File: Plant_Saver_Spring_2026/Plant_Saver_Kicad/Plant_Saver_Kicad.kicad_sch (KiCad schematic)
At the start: 23 parts, among them J2 StripboardConn, Q9 G09P02L, SW1 Select, SW2 Select, SW8 NK236WH, U1 CDBA140SL-HF, U2 CDBA140SL-HF, U3 CDBA140SL-HF, U4 CDBA140SL-HF, U5 ESP32-WROOM-32E-N16, U8 ESP32-WROOM-32D

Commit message: Misc. changes
Updated peripheral power switch, UI board connections
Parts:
- removed J2: StripboardConn, symbol Connector:Conn_01x08_Socket
- added J4, J6: B8B-PH-K-SLFSN, CONN_B8B-PH-K-S_JST, symbol B8B_PH_K_S_LF__SN_:B8B-PH-K-SLFSN
- added Q13: G09P02L, G09P02L:TSOT-23, symbol Simulation_SPICE:PMOS
- added R14: 150K, Resistor_THT:R_Axial_DIN0207_L6.3mm_D2.5mm_P10.16mm_Horizontal, symbol Device:R_US
- R10: value 150K -> 100K
- SW8: value NK236WH -> 25336NA; footprint NK236WH:SW_Slide-03_APEM-NK23GWH_10x9.2x2.6_P2.54mm -> 25336NA:SWITCH_25336NA_APM
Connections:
- net Error: now also J6.3
- net GND: now also J6.8, R14.2
- net Periph_EN: now also Q13.2 (G); no longer Q9.2 (G)
- net Vbus: now also Q13.3 (S)
- net at U5.11 (IO26): now also J6.4
- net at U5.12 (IO27): now also J6.5
- net at U5.13 (IO14): now also J6.6
- net at U5.14 (IO12): now also J6.7
- new net: Q13.1 (D), Q9.2 (G), R14.1
- new net Interface Stripboard/Chg_Cpt_Lt: J4.2
- new net Interface Stripboard/Chg_Lt: J4.1
- new net Interface Stripboard/Chg_Scr_Btn: J4.6
- new net Interface Stripboard/Down_Btn: J4.5
- new net Interface Stripboard/Error_Lt: J4.3
- new net Interface Stripboard/GND: J4.8
- new net Interface Stripboard/Sel_Btn: J4.7
- new net Interface Stripboard/Up_Btn: J4.4
- new net STAT1: J6.1
- new net STAT2: J6.2
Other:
- sheet Interface Stripboard ports: added Chg_Cpt_Lt, Chg_Lt, Chg_Scr_Btn, Down_Btn, Error_Lt, GND, Sel_Btn, Up_Btn; removed none
- note removed: "This is Dumb, Replace w/ NMOS on negative side"
- moved on the sheet: U8

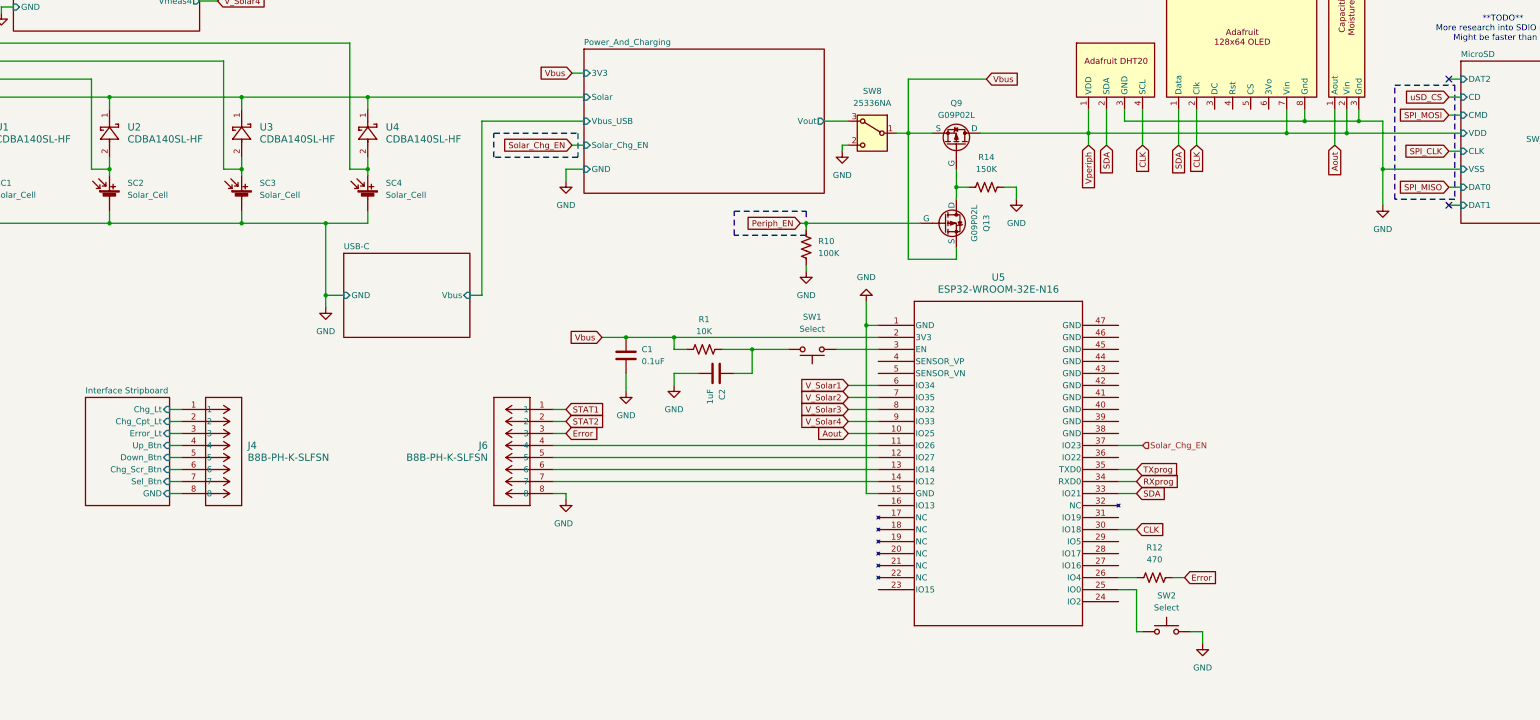
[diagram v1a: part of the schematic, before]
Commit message: Misc. fixes to schematic
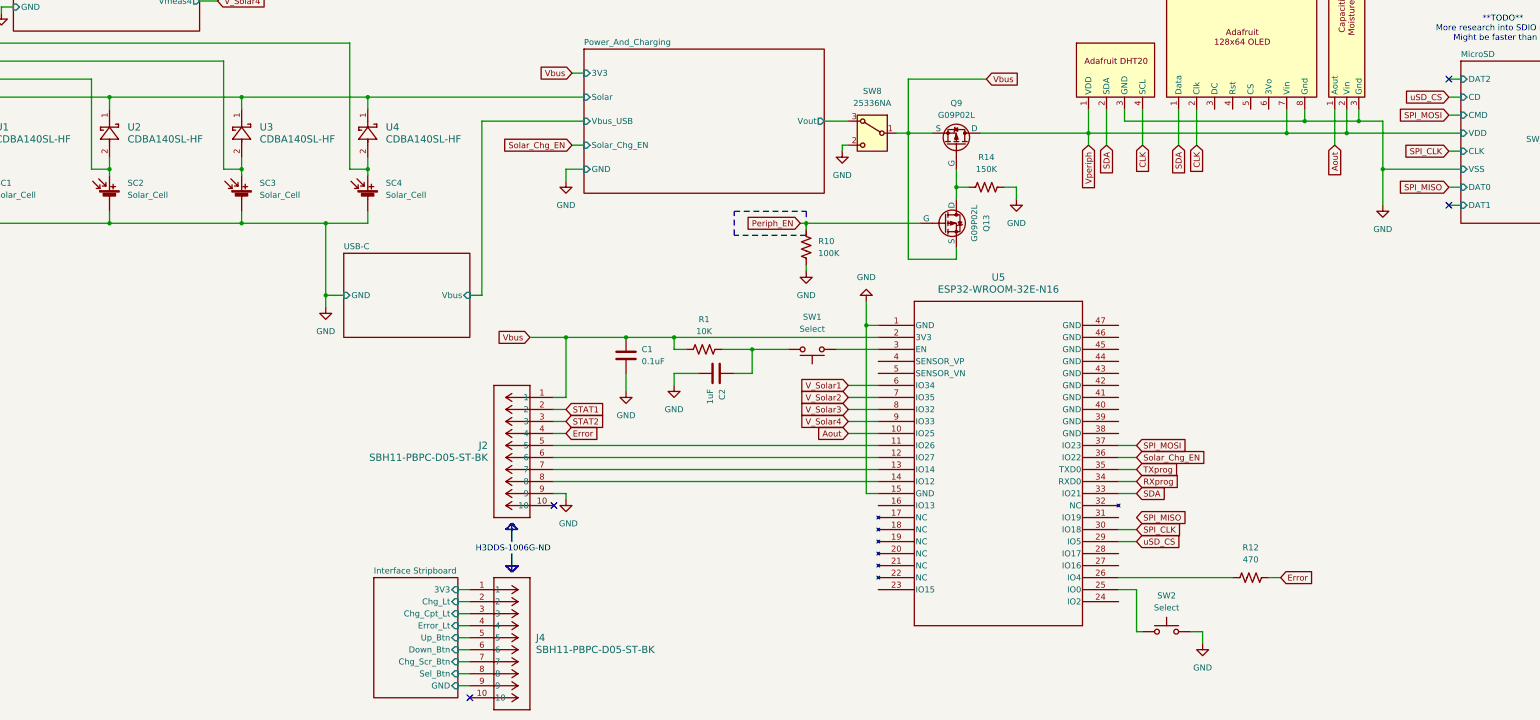
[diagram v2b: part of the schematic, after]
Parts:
- removed J4, J6: B8B-PH-K-SLFSN, CONN_B8B-PH-K-S_JST, symbol B8B_PH_K_S_LF__SN_:B8B-PH-K-SLFSN
- added J2, J4: SBH11-PBPC-D05-ST-BK, CONN_SBH11-PBPC-D05-ST-BK_SUL, symbol SBH11_PBPC_D05_ST_BK:SBH11-PBPC-D05-ST-BK
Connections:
- net CLK: no longer U5.30 (IO18)
- net Error: now also J2.4
- net GND: now also J2.9
- net Interface Stripboard/Chg_Cpt_Lt: now also J4.3
- net Interface Stripboard/Chg_Lt: now also J4.2
- net Interface Stripboard/Chg_Scr_Btn: now also J4.7
- net Interface Stripboard/Down_Btn: now also J4.6
- net Interface Stripboard/Error_Lt: now also J4.4
- net Interface Stripboard/GND: now also J4.9
- net Interface Stripboard/Sel_Btn: now also J4.8
- net Interface Stripboard/Up_Btn: now also J4.5
- net SPI_CLK: now also U5.30 (IO18)
- net SPI_MOSI: now also U5.37 (IO23)
- net STAT1: now also J2.2
- net STAT2: now also J2.3
- net Solar_Chg_EN: now also U5.36 (IO22); no longer U5.37 (IO23)
- net Vbus: now also J2.1
- net uSD_CS: now also U5.29 (IO5)
- net at U5.11 (IO26): now also J2.5
- net at U5.12 (IO27): now also J2.6
- net at U5.13 (IO14): now also J2.7
- net at U5.14 (IO12): now also J2.8
- new net Interface Stripboard/3V3: J4.1
- no-connect marks 2 -> 4
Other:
- sheet Interface Stripboard ports: added 3V3; removed none
- note added: "H3DDS-1006G-ND"
- moved on the sheet: R12

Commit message: Footprint updates
Misc. schematic fixes, mostly updated/added footprints where needed.
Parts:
- removed R12: 470, Resistor_THT:R_Axial_DIN0207_L6.3mm_D2.5mm_P10.16mm_Horizontal, symbol Device:R_US
- added C10: 0.1uF, Capacitor_THT:C_Disc_D4.7mm_W2.5mm_P5.00mm, symbol Device:C
- added C11: 10uF, Capacitor_THT:C_Disc_D4.7mm_W2.5mm_P5.00mm, symbol Device:C
- added J5: S3B-PH-K-S, Connector_JST:JST_PH_S3B-PH-K_1x03_P2.00mm_Horizontal, symbol Connector:Conn_01x03_Pin
- added J6, J7: SM04B-SRSS-TB, Connector_JST:JST_SH_SM04B-SRSS-TB_1x04-1MP_P1.00mm_Horizontal, symbol Connector:Conn_01x04_Pin
- SW1: value Select -> Reset; footprint (none) -> Button_Switch_THT:SW_PUSH_6mm
- SW2: value Select -> Boot; footprint (none) -> Button_Switch_THT:SW_PUSH_6mm
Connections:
- net Aout: now also J5.1 (Pin_1); no longer U9.1 (Aout)
- net CLK: now also J6.4 (Pin_4); no longer U7.2 (Clk)
- net Error: now also U5.26 (IO4)
- net GND: now also C2.1, SW1.1, C10.2, C11.2, J5.3 (Pin_3), J6.1 (Pin_1); no longer C2.2, U7.8 (Gnd), U9.3 (Gnd)
- net SDA: now also J6.3 (Pin_3); no longer U7.1 (Data)
- net Vbus: now also R1.2, C11.1; no longer R1.1
- net Vperiph: now also J5.2 (Pin_2), J6.2 (Pin_2); no longer U7.7 (Vin), U9.2 (Vin)
- net at U5.3 (EN): now also C2.2, R1.1, SW1.2, C10.1; no longer SW1.1
- new net: J7.1 (Pin_1), U7.8 (Gnd)
- new net: J7.2 (Pin_2), U7.7 (Vin)
- new net: J7.3 (Pin_3), U7.1 (Data)
- new net: J7.4 (Pin_4), U7.2 (Clk)
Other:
- sheet Power_And_Charging ports: added STAT1, STAT2; removed none
- note added: "1528-4210-ND"
- note added: "A03KR03KR26E152B"
- note added: "STEMMA QT Pinout: 1 [BLK] - GND 2 [RED] - Vcc 3 [BLU] - SDA 4 [YEL] - SCL"
- moved on the sheet: C1, C2, J2, J4, Q13, Q9, R1, R10, R14, SC1, SC2, SC3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

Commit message: Programming ports on schematic
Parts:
- removed U8: ESP32-WROOM-32D, RF_Module:ESP32-WROOM-32D, symbol RF_Module:ESP32-WROOM-32D
- added J8: Conn_01x06_Socket, Connector_PinSocket_2.54mm:PinSocket_1x06_P2.54mm_Vertical, symbol Connector:Conn_01x06_Socket
- added J9: Conn_01x02_Pin, Connector_PinHeader_2.54mm:PinHeader_1x02_P2.54mm_Vertical, symbol Connector:Conn_01x02_Pin
- added R19: 10K, Resistor_THT:R_Axial_DIN0207_L6.3mm_D2.5mm_P10.16mm_Horizontal, symbol Device:R_US
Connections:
- net GND: now also J8.1 (Pin_1), R19.1
- net Periph_EN: now also U5.28 (IO17)
- net SPI_MISO: now also U5.31 (IO19)
- net Solar_Chg_EN: now also U5.16 (IO13); no longer U5.36 (IO22)
- net Vbus: now also J9.1 (Pin_1)
- net uSD_DET: now also U5.27 (IO16)
- net at U5.24 (IO2): now also R19.2
- net CLK renamed SCL
- net SCL: now also U5.36 (IO22)
- net RXprog: no longer names the net of U5.34 (RXD0)
- net RXprog: now also J8.4 (Pin_4)
- net TXprog: no longer names the net of U5.35 (TXD0)
- net TXprog: now also J8.5 (Pin_5)
- new net: J8.3 (Pin_3), J9.2 (Pin_2)
- no-connect marks 4 -> 6
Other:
- note added: "FTDI Board Pinout: GND CTS Vcc Tx Rx DTR"
- note added: "Jumper for powering chip from FTDI"
- note removed: "**TODO** More research into SDIO needed Might be faster than SPI"
- note removed: "Most LIPO charging chips use current detection to end charging, since the battery will draw very little current when it's at full voltage. If the system load is also connected to that pin, it can throw that sensing out of wack since the current draw isn't only from the battery anymore."
- moved on the sheet: SW2

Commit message: Started PCB
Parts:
- added TP1, TP2, TP3, TP4, TP5, TP6: TestPoint, TestPoint:TestPoint_Pad_1.5x1.5mm, symbol Connector:TestPoint
- J2: footprint CONN_SBH11-PBPC-D05-ST-BK_SUL -> SBH11_PBPC_D05_ST_BK:CONN_SBH11-PBPC-D05-ST-BK_SUL
- U1, U2, U3, U4: footprint (none) -> CDBA140SL_HF:CDBA-HF
- renumbered C11 to C2, C2 to C3, C10 to C4, J4 to J1, J6 to J3, J7 to J4, J9 to J5, J8 to J6, J5 to J7, Q13 to Q1, Q9 to Q2, R10 to R2, R14 to R3, R19 to R4, SW8 to SW2, SW2 to SW3, U9 to U8
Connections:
- net GND: now also TP1.1
- net Power_And_Charging/Solar: now also TP2.1
- net SCL: now also TP4.1
- net SDA: now also TP3.1
- net at J6.4 (Pin_4), U5.34 (RXD0): now also TP6.1
- net at J6.5 (Pin_5), U5.35 (TXD0): now also TP5.1

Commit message: Refined PCB layout
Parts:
- added R44, R45: 10K, Resistor_SMD:R_1206_3216Metric_Pad1.30x1.75mm_HandSolder, symbol Device:R_US
- C1, C2, C3, C4: footprint Capacitor_THT:C_Disc_D4.7mm_W2.5mm_P5.00mm -> Capacitor_SMD:C_1206_3216Metric_Pad1.33x1.80mm_HandSolder
- R1, R2, R3, R4: footprint Resistor_THT:R_Axial_DIN0207_L6.3mm_D2.5mm_P10.16mm_Horizontal -> Resistor_SMD:R_1206_3216Metric_Pad1.30x1.75mm_HandSolder
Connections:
- net SCL: now also R44.2
- net SDA: now also R45.2
- net Vperiph: now also R44.1, R45.1
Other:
- moved on the sheet: J5, J6, TP3, TP4, TP5, TP6

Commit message: Began PCB routing
Routed solar input, measurement and protections
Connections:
- net GND: now also U5.38 (GND), U5.39 (GND), U5.40 (GND), U5.41 (GND), U5.42 (GND), U5.43 (GND), U5.44 (GND), U5.45 (GND), U5.46 (GND), U5.47 (GND)
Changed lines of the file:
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@@
 	)
 	(junction
+		(at 287.02 180.34)
+		(diameter 0)
+		(color 0 0 0 0)
+	)
+	(junction
 		(at 287.02 127)
 		(diameter 0)
@@
 	)
 	(junction
+		(at 287.02 162.56)
+		(diameter 0)
+		(color 0 0 0 0)
+	)
+	(junction
 		(at 302.26 124.46)
 		(diameter 0)
@@
 	)
 	(junction
+		(at 287.02 167.64)
+		(diameter 0)
+		(color 0 0 0 0)
+	)
+	(junction
 		(at 128.27 114.3)
 		(diameter 0)
@@
 	)
 	(junction
+		(at 287.02 177.8)
+		(diameter 0)
+		(color 0 0 0 0)
+	)
+	(junction
+		(at 287.02 165.1)
+		(diameter 0)
+		(color 0 0 0 0)
+	)
+	(junction
 		(at 193.04 167.64)
 		(diameter 0)
@@
 	)
 	(junction
+		(at 287.02 182.88)
+		(diameter 0)
+		(color 0 0 0 0)
+	)
+	(junction
+		(at 287.02 175.26)
+		(diameter 0)
+		(color 0 0 0 0)
+	)
+	(junction
 		(at 302.26 137.16)
 		(diameter 0)
@@
 	)
 	(junction
+		(at 287.02 172.72)
+		(diameter 0)
+		(color 0 0 0 0)
+	)
+	(junction
+		(at 287.02 170.18)
+		(diameter 0)
+		(color 0 0 0 0)
+	)
+	(junction
 		(at 73.66 114.3)
 		(diameter 0)
@@
 		)
 	)
+	(wire
+		(pts
+			(xy 287.02 180.34) (xy 287.02 177.8)
+		)
+		(stroke
+			(width 0)
+			(type default)
+		)
+	)
 	(polyline
 		(pts
@@
 	(wire
 		(pts
+			(xy 287.02 172.72) (xy 287.02 170.18)
+		)
+		(stroke
+			(width 0)
+			(type default)
+		)
+	)
+	(wire
+		(pts
 			(xy 134.62 238.76) (xy 137.16 238.76)
 		)
@@
 	(wire
 		(pts
+			(xy 287.02 160.02) (xy 292.1 160.02)
+		)
+		(stroke
+			(width 0)
+			(type default)
+		)
+	)
+	(wire
+		(pts
 			(xy 252.73 133.35) (xy 252.73 135.89)
 		)
@@
 		)
 	)
+	(wire
+		(pts
+			(xy 287.02 167.64) (xy 287.02 165.1)
+		)
+		(stroke
+			(width 0)
+			(type default)
+		)
+	)
 	(polyline
 		(pts
@@
 	(wire
 		(pts
+			(xy 287.02 165.1) (xy 287.02 162.56)
+		)
+		(stroke
+			(width 0)
+			(type default)
+		)
+	)
+	(wire
+		(pts
 			(xy 298.45 74.93) (xy 298.45 72.39)
 		)
@@
 	(wire
 		(pts
+			(xy 292.1 160.02) (xy 292.1 162.56)
+		)
+		(stroke
+			(width 0)
+			(type default)
+		)
+	)
+	(wire
+		(pts
 			(xy 303.53 74.93) (xy 298.45 74.93)
 		)
@@
 	(wire
 		(pts
+			(xy 287.02 177.8) (xy 287.02 175.26)
+		)
+		(stroke
+			(width 0)
+			(type default)
+		)
+	)
+	(wire
+		(pts
 			(xy 306.07 77.47) (xy 294.64 77.47)
 		)
@@
 	(wire
 		(pts
+			(xy 287.02 162.56) (xy 287.02 160.02)
+		)
+		(stroke
+			(width 0)
+			(type default)
+		)
+	)
+	(wire
+		(pts
 			(xy 134.62 223.52) (xy 137.16 223.52)
 		)
@@
 	(wire
 		(pts
+			(xy 287.02 170.18) (xy 287.02 167.64)
+		)
+		(stroke
+			(width 0)
+			(type default)
+		)
+	)
+	(wire
+		(pts
 			(xy 134.62 231.14) (xy 137.16 231.14)
 		)
@@
 	(wire
 		(pts
+			(xy 287.02 185.42) (xy 287.02 182.88)
+		)
+		(stroke
+			(width 0)
+			(type default)
+		)
+	)
+	(wire
+		(pts
 			(xy 154.94 190.5) (xy 236.22 190.5)
 		)
@@
 		)
 	)
+	(wire
+		(pts
+			(xy 287.02 175.26) (xy 287.02 172.72)
+		)
+		(stroke
+			(width 0)
+			(type default)
+		)
+	)
 	(polyline
 		(pts
@@
 		)
 	)
+	(wire
+		(pts
+			(xy 287.02 182.88) (xy 287.02 180.34)
+		)
+		(stroke
+			(width 0)
+			(type default)
+		)
+	)
 	(global_label "SCL"
 		(shape input)
@@
 					(unit 1)
 				)
+			)
+		)
+	)
+	(symbol
+		(lib_id "power:GND")
+		(at 292.1 162.56 0)
+		(unit 1)
+		(exclude_from_sim no)
+		(in_bom yes)
+		(on_board yes)
+		(dnp no)
+		(fields_autoplaced yes)
+		(property "Reference" "#PWR022"
+			(at 292.1 168.91 0)
+			(effects
+				(font
+					(size 1.27 1.27)
+				)
+				(hide yes)
+			)
+		)
+		(property "Value" "GND"
+			(at 292.1 167.64 0)
+			(effects
+				(font
+					(size 1.27 1.27)
+				)
+			)
+		)
+		(property "Footprint" ""
+			(at 292.1 162.56 0)
+			(effects
+				(font
+					(size 1.27 1.27)
+				)
+				(hide yes)
+			)
+		)
+		(property "Datasheet" ""
+			(at 292.1 162.56 0)
+			(effects
+				(font
+					(size 1.27 1.27)
+				)
+				(hide yes)
+			)
+		)
+		(property "Description" "Power symbol creates a global label with name \"GND\" , ground"
+			(at 292.1 162.56 0)
+			(effects
+				(font
+					(size 1.27 1.27)
+				)
+				(hide yes)
+			)
+		)
+		(pin "1"
+		)
+		(instances
+			(project "Plant_Saver_Kicad"
+				(path "/7f244634-d37a-4ff0-ba36-8027330ab1bd"
+					(reference "#PWR022")
+					(unit 1)
+				)

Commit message: Re-routed to fix issue on schematic
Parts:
- added J11: Test, Connector_PinHeader_2.54mm:PinHeader_1x02_P2.54mm_Vertical, symbol Connector:Conn_01x02_Socket
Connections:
- net Power_And_Charging/Vout: now also J11.2 (Pin_2)
- net Vbus: now also J11.1 (Pin_1)
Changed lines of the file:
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@@
 	)
 	(junction
+		(at 226.06 119.38)
+		(diameter 0)
+		(color 0 0 0 0)
+	)
+	(junction
 		(at 303.53 119.38)
 		(diameter 0)
@@
 	)
 	(junction
+		(at 240.03 121.92)
+		(diameter 0)
+		(color 0 0 0 0)
+	)
+	(junction
 		(at 101.6 114.3)
 		(diameter 0)
@@
 	(wire
 		(pts
+			(xy 226.06 119.38) (xy 229.87 119.38)
+		)
+		(stroke
+			(width 0)
+			(type default)
+		)
+	)
+	(wire
+		(pts
 			(xy 356.87 137.16) (xy 359.41 137.16)
 		)
@@
 	(wire
 		(pts
+			(xy 240.03 121.92) (xy 240.03 132.08)
+		)
+		(stroke
+			(width 0)
+			(type default)
+		)
+	)
+	(wire
+		(pts
 			(xy 289.56 229.87) (xy 313.69 229.87)
 		)
@@
 	(wire
 		(pts
-			(xy 224.79 119.38) (xy 229.87 119.38)
+			(xy 224.79 119.38) (xy 226.06 119.38)
 		)
 		(stroke
@@
 	(wire
 		(pts
+			(xy 240.03 132.08) (xy 236.22 132.08)
+		)
+		(stroke
+			(width 0)
+			(type default)
+		)
+	)
+	(wire
+		(pts
 			(xy 287.02 193.04) (xy 302.26 193.04)
 		)
@@
 	(wire
 		(pts
+			(xy 226.06 132.08) (xy 233.68 132.08)
+		)
+		(stroke
+			(width 0)
+			(type default)
+		)
+	)
+	(wire
+		(pts
 			(xy 287.02 162.56) (xy 287.02 160.02)
 		)
@@
 		)
 	)
+	(wire
+		(pts
+			(xy 226.06 119.38) (xy 226.06 132.08)
+		)
+		(stroke
+			(width 0)
+			(type default)
+		)
+	)
 	(polyline
 		(pts
@@
 					(unit 1)
 				)
+			)
+		)
+	)
+	(symbol
+		(lib_id "Connector:Conn_01x02_Socket")
+		(at 236.22 137.16 270)
+		(unit 1)
+		(exclude_from_sim no)
+		(in_bom yes)
+		(on_board yes)
+		(dnp no)
+		(fields_autoplaced yes)
+		(property "Reference" "J11"
+			(at 237.49 135.2549 90)
+			(effects
+				(font
+					(size 1.27 1.27)
+				)
+				(justify left)
+			)
+		)
+		(property "Value" "Test"
+			(at 237.49 137.7949 90)
+			(effects
+				(font
+					(size 1.27 1.27)
+				)
+				(justify left)
+			)
+		)
+		(property "Footprint" "Connector_PinHeader_2.54mm:PinHeader_1x02_P2.54mm_Vertical"
+			(at 236.22 137.16 0)
+			(effects
+				(font
+					(size 1.27 1.27)
+				)
+				(hide yes)
+			)
+		)
+		(property "Datasheet" "~"
+			(at 236.22 137.16 0)
+			(effects
+				(font
+					(size 1.27 1.27)
+				)
+				(hide yes)
+			)
+		)
+		(property "Description" "Generic connector, single row, 01x02, script generated"
+			(at 236.22 137.16 0)
+			(effects
+				(font
+					(size 1.27 1.27)
+				)
+				(hide yes)
+			)
+		)
+		(pin "1"
+		)
+		(pin "2"
+		)
+		(instances
+			(project ""
+				(path "/7f244634-d37a-4ff0-ba36-8027330ab1bd"
+					(reference "J11")
+					(unit 1)
+				)
